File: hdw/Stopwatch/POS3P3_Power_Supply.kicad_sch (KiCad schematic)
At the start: 13 parts, among them U301 TPS62130

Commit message: started sch work
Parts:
- removed C304, C305: 22uF, Capacitors_SMD:C_1206, symbol Custom_Library:C_Custom
- added C? (x2): 10uF, Capacitors_SMD:C_1206, symbol Custom_Library:C_Custom
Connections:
- net +3V3: now also C?.1, C?.1
- net GND: now also C?.2, C?.2
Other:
- moved on the sheet: C301, C302, C303, R302, R305, TP301, U301

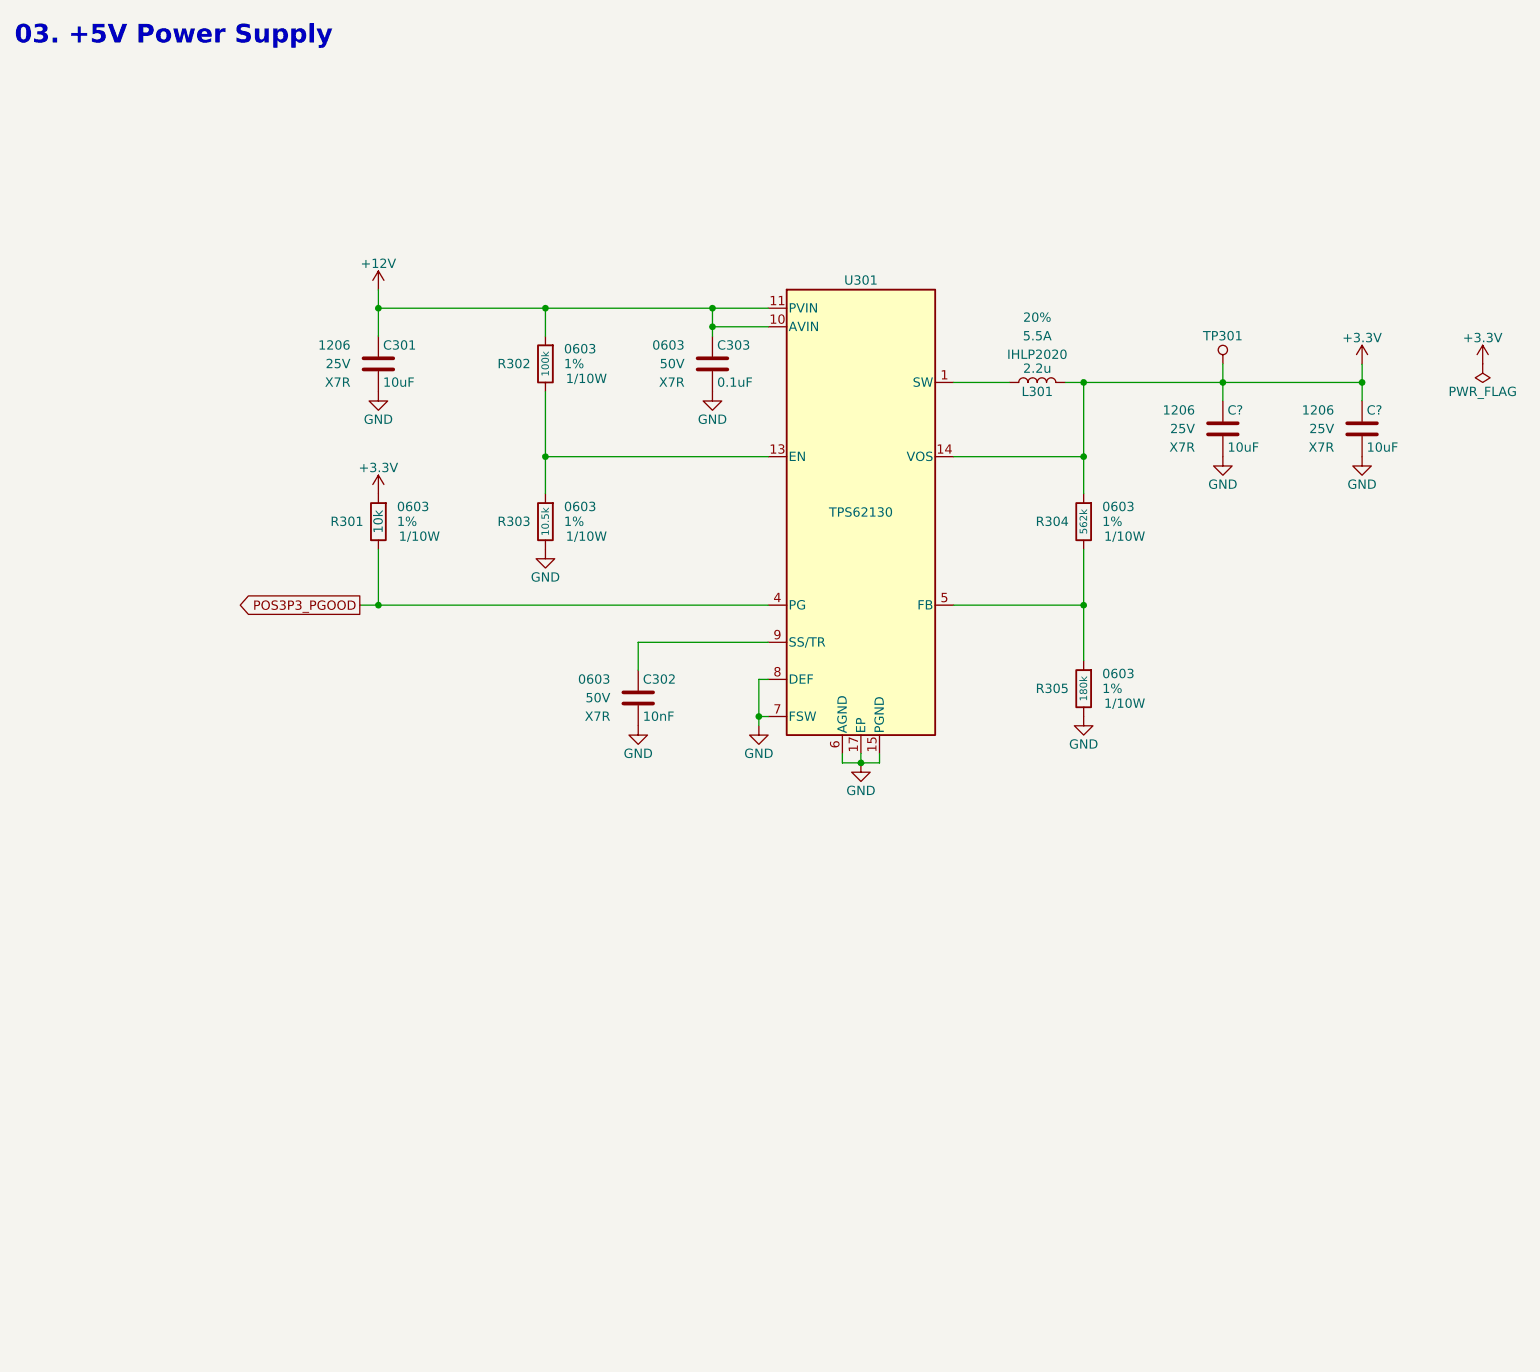
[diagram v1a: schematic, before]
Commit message: adjusted stage sheet
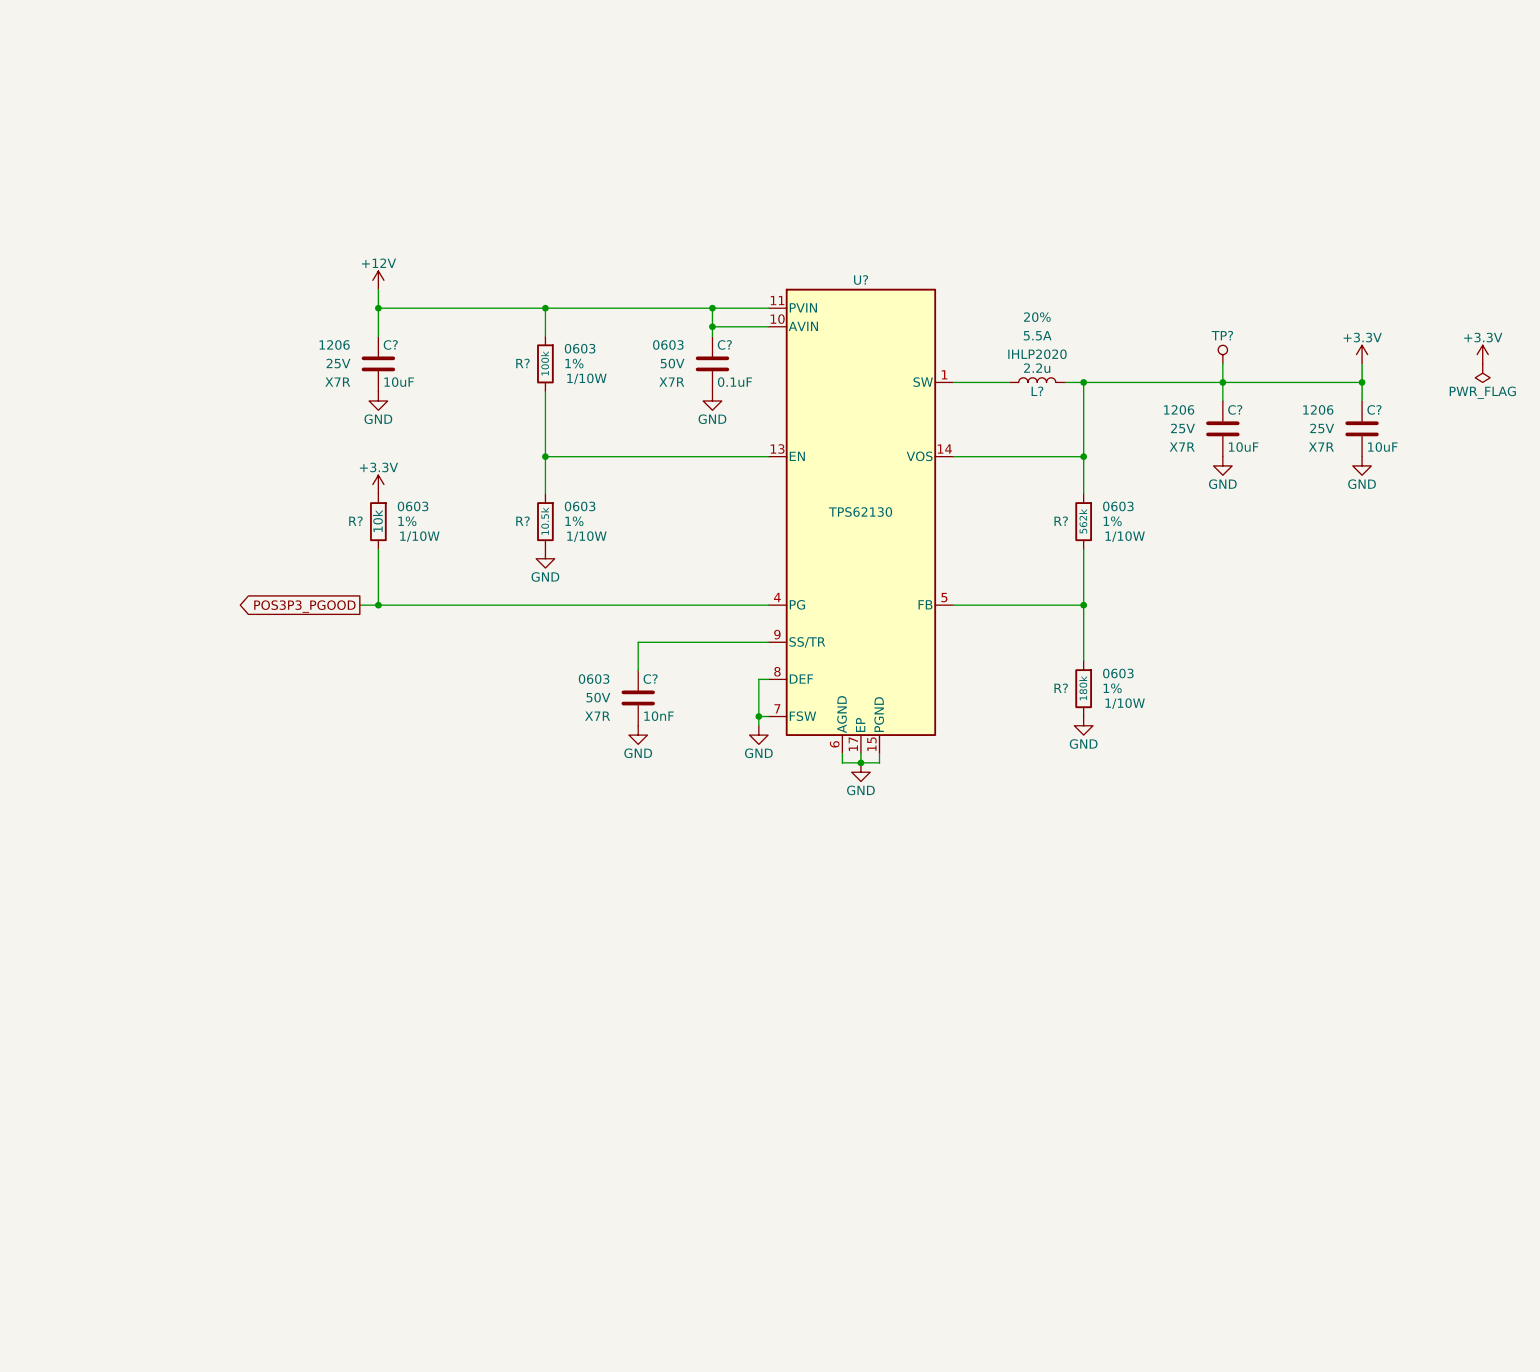
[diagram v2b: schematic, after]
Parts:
- renumbered C303 to C?, C301 to C?, C302 to C?, L301 to L?, R302 to R?, R301 to R?, R304 to R?, R305 to R?, R303 to R?, TP301 to TP?, U301 to U?
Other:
- note removed: "03. +5V Power Supply"

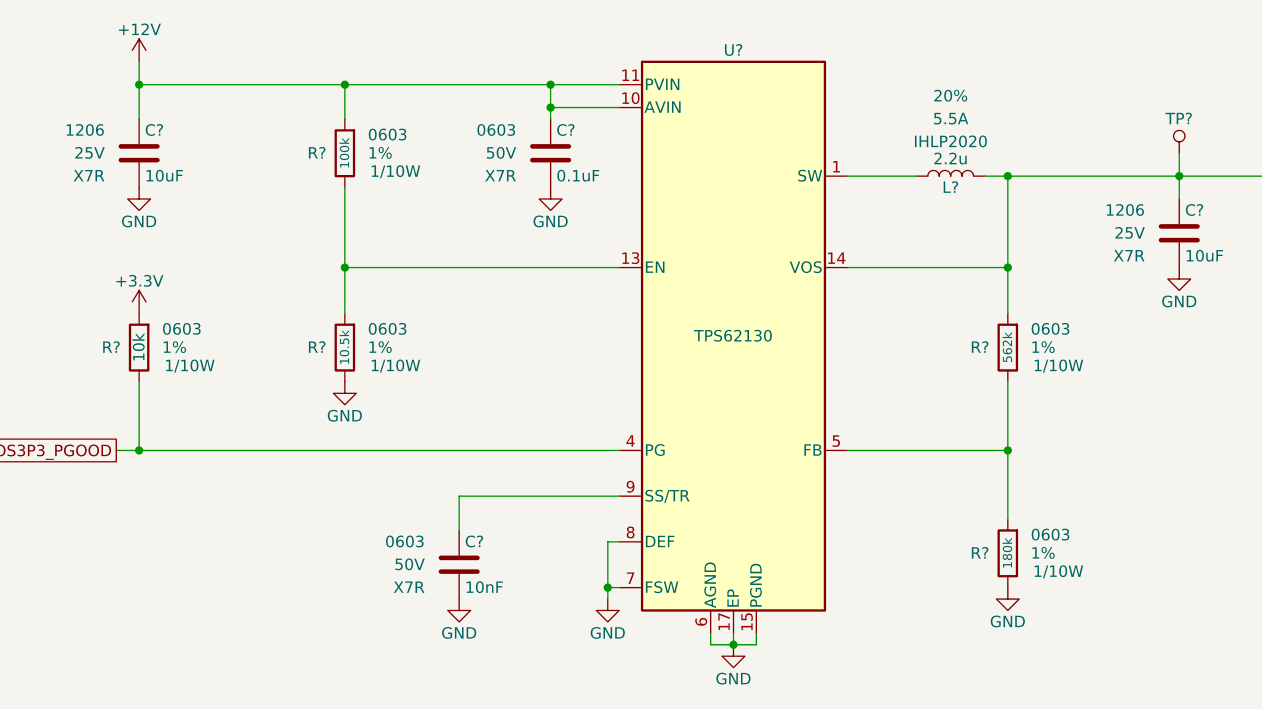
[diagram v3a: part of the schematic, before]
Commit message: Assigned some digikey pns
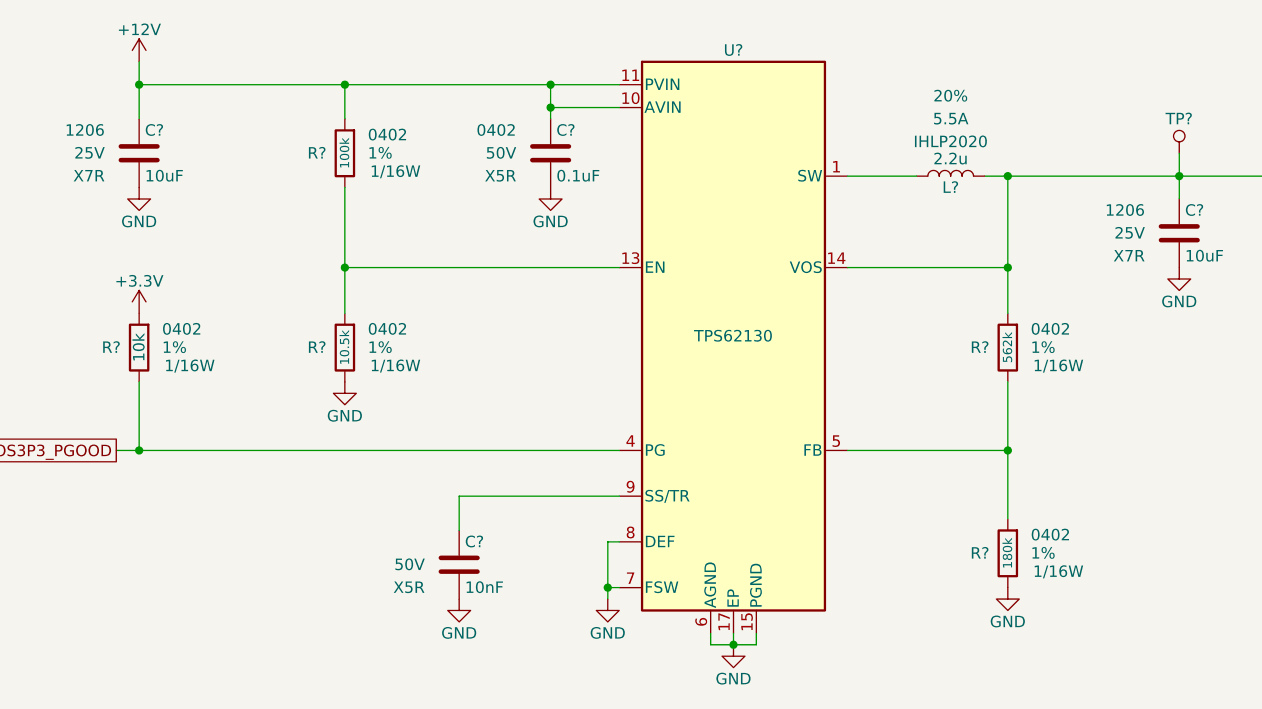
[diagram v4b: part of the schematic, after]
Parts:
- C?: footprint Capacitors_SMD:C_0603 -> Capacitors_SMD:C_0402; Dielectric X7R -> X5R; Digi-Key PN 490-8020-1-ND -> 490-10697-1-ND; display_footprint 0603 -> 0402
- C?: footprint Capacitors_SMD:C_0603 -> Capacitors_SMD:C_0402; Dielectric X7R -> X5R; Digi-Key PN 1276-1921-1-ND -> 445-12201-1-ND; display_footprint 0603 -> (none)
- R?: footprint Resistors_SMD:R_0603 -> Resistors_SMD:R_0402; Digi-Key PN A106046CT-ND -> RMCF0402FT100KCT-ND; Wattage 1/10W -> 1/16W; display_footprint 0603 -> 0402
- R?: footprint Resistors_SMD:R_0603 -> Resistors_SMD:R_0402; Digi-Key PN RHM10KADCT-ND -> RMCF0402FT10K0CT-ND; Wattage 1/10W -> 1/16W; display_footprint 0603 -> 0402
- R?: footprint Resistors_SMD:R_0603 -> Resistors_SMD:R_0402; Digi-Key PN 311-562KHRCT-ND -> RMCF0402FT562KCT-ND; Wattage 1/10W -> 1/16W; display_footprint 0603 -> 0402
- R?: footprint Resistors_SMD:R_0603 -> Resistors_SMD:R_0402; Digi-Key PN 749-1763-1-ND -> RMCF0402FT180KCT-ND; Wattage 1/10W -> 1/16W; display_footprint 0603 -> 0402
- R?: footprint Resistors_SMD:R_0603 -> Resistors_SMD:R_0402; Digi-Key PN 311-10.5KHRCT-ND -> RMCF0402FT10K5CT-ND; Wattage 1/10W -> 1/16W; display_footprint 0603 -> 0402
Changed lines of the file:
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@@
       (effects (font (size 1.27 1.27)) (justify left))
     )
-    (property "Footprint" "Capacitors_SMD:C_0603" (at 110.1852 64.77 0)
+    (property "Footprint" "Capacitors_SMD:C_0402" (at 110.1852 64.77 0)
       (effects (font (size 1.27 1.27)) hide)
     )
@@
       (effects (font (size 1.27 1.27)) hide)
     )
-    (property "display_footprint" "0603" (at 105.41 58.42 0)
+    (property "display_footprint" "0402" (at 105.41 58.42 0)
       (effects (font (size 1.27 1.27)) (justify right))
     )
@@
       (effects (font (size 1.27 1.27)) (justify right))
     )
-    (property "Dielectric" "X7R" (at 105.41 63.5 0)
-      (effects (font (size 1.27 1.27)) (justify right))
-    )
-    (property "Digi-Key PN" "490-8020-1-ND" (at 120.015 48.26 0)
+    (property "Dielectric" "X5R" (at 105.41 63.5 0)
+      (effects (font (size 1.27 1.27)) (justify right))
+    )
+    (property "Digi-Key PN" "490-10697-1-ND" (at 120.015 48.26 0)
       (effects (font (size 1.524 1.524)) hide)
     )
@@
       (effects (font (size 1.016 1.016)))
     )
-    (property "Footprint" "Resistors_SMD:R_0603" (at 86.36 60.96 0)
+    (property "Footprint" "Resistors_SMD:R_0402" (at 86.36 60.96 0)
       (effects (font (size 1.27 1.27)) hide)
     )
@@
       (effects (font (size 1.27 1.27)) hide)
     )
-    (property "display_footprint" "0603" (at 88.9 58.928 0)
+    (property "display_footprint" "0402" (at 88.9 58.928 0)
       (effects (font (size 1.27 1.27)) (justify left))
     )
@@
       (effects (font (size 1.27 1.27)) (justify left))
     )
-    (property "Wattage" "1/10W" (at 89.154 62.992 0)
-      (effects (font (size 1.27 1.27)) (justify left))
-    )
-    (property "Digi-Key PN" "A106046CT-ND" (at 0 122.428 0)
+    (property "Wattage" "1/16W" (at 89.154 62.992 0)
+      (effects (font (size 1.27 1.27)) (justify left))
+    )
+    (property "Digi-Key PN" "RMCF0402FT100KCT-ND" (at 0 122.428 0)
       (effects (font (size 1.27 1.27)) hide)
     )
@@
       (effects (font (size 1.27 1.27)))
     )
-    (property "Footprint" "Resistors_SMD:R_0603" (at 63.5 82.55 0)
+    (property "Footprint" "Resistors_SMD:R_0402" (at 63.5 82.55 0)
       (effects (font (size 1.27 1.27)) hide)
     )
@@
       (effects (font (size 1.27 1.27)) hide)
     )
-    (property "display_footprint" "0603" (at 66.04 80.518 0)
+    (property "display_footprint" "0402" (at 66.04 80.518 0)
       (effects (font (size 1.27 1.27)) (justify left))
     )
@@
       (effects (font (size 1.27 1.27)) (justify left))
     )
-    (property "Wattage" "1/10W" (at 66.294 84.582 0)
-      (effects (font (size 1.27 1.27)) (justify left))
-    )
-    (property "Digi-Key PN" "RHM10KADCT-ND" (at 71.12 72.39 0)
+    (property "Wattage" "1/16W" (at 66.294 84.582 0)
+      (effects (font (size 1.27 1.27)) (justify left))
+    )
+    (property "Digi-Key PN" "RMCF0402FT10K0CT-ND" (at 71.12 72.39 0)
       (effects (font (size 1.524 1.524)) hide)
     )
@@
       (effects (font (size 1.27 1.27)) (justify left))
     )
-    (property "Footprint" "Capacitors_SMD:C_0603" (at 100.0252 110.49 0)
+    (property "Footprint" "Capacitors_SMD:C_0402" (at 100.0252 110.49 0)
       (effects (font (size 1.27 1.27)) hide)
     )
@@
       (effects (font (size 1.27 1.27)) hide)
     )
-    (property "display_footprint" "0603" (at 95.25 104.14 0)
+    (property "display_footprint" "" (at 95.25 104.14 0)
       (effects (font (size 1.27 1.27)) (justify right))
     )
@@
       (effects (font (size 1.27 1.27)) (justify right))
     )
-    (property "Dielectric" "X7R" (at 95.25 109.22 0)
-      (effects (font (size 1.27 1.27)) (justify right))
-    )
-    (property "Digi-Key PN" "1276-1921-1-ND" (at -0.508 213.868 0)
+    (property "Dielectric" "X5R" (at 95.25 109.22 0)
+      (effects (font (size 1.27 1.27)) (justify right))
+    )
+    (property "Digi-Key PN" "445-12201-1-ND" (at -0.508 213.868 0)
       (effects (font (size 1.27 1.27)) hide)
     )
@@
       (effects (font (size 1.016 1.016)))
     )
-    (property "Footprint" "Resistors_SMD:R_0603" (at 160.02 82.55 0)
+    (property "Footprint" "Resistors_SMD:R_0402" (at 160.02 82.55 0)
       (effects (font (size 1.27 1.27)) hide)
     )
@@
       (effects (font (size 1.27 1.27)) hide)
     )
-    (property "display_footprint" "0603" (at 162.56 80.518 0)
+    (property "display_footprint" "0402" (at 162.56 80.518 0)
       (effects (font (size 1.27 1.27)) (justify left))
     )
@@
       (effects (font (size 1.27 1.27)) (justify left))
     )
-    (property "Wattage" "1/10W" (at 162.814 84.582 0)
-      (effects (font (size 1.27 1.27)) (justify left))
-    )
-    (property "Digi-Key PN" "311-562KHRCT-ND" (at 160.02 82.55 0)
+    (property "Wattage" "1/16W" (at 162.814 84.582 0)
+      (effects (font (size 1.27 1.27)) (justify left))
+    )
+    (property "Digi-Key PN" "RMCF0402FT562KCT-ND" (at 160.02 82.55 0)
       (effects (font (size 1.27 1.27)) hide)
     )
@@
       (effects (font (size 1.016 1.016)))
     )
-    (property "Footprint" "Resistors_SMD:R_0603" (at 160.02 105.41 0)
+    (property "Footprint" "Resistors_SMD:R_0402" (at 160.02 105.41 0)
       (effects (font (size 1.27 1.27)) hide)
     )
@@
       (effects (font (size 1.27 1.27)) hide)
     )
-    (property "display_footprint" "0603" (at 162.56 103.378 0)
+    (property "display_footprint" "0402" (at 162.56 103.378 0)
       (effects (font (size 1.27 1.27)) (justify left))
     )
@@
       (effects (font (size 1.27 1.27)) (justify left))
     )
-    (property "Wattage" "1/10W" (at 162.814 107.442 0)
-      (effects (font (size 1.27 1.27)) (justify left))
-    )
-    (property "Digi-Key PN" "749-1763-1-ND" (at 160.02 105.41 0)
+    (property "Wattage" "1/16W" (at 162.814 107.442 0)
+      (effects (font (size 1.27 1.27)) (justify left))
+    )
+    (property "Digi-Key PN" "RMCF0402FT180KCT-ND" (at 160.02 105.41 0)
       (effects (font (size 1.27 1.27)) hide)
     )
@@
       (effects (font (size 1.016 1.016)))
     )
-    (property "Footprint" "Resistors_SMD:R_0603" (at 86.36 82.55 0)
+    (property "Footprint" "Resistors_SMD:R_0402" (at 86.36 82.55 0)
       (effects (font (size 1.27 1.27)) hide)
     )
@@
       (effects (font (size 1.27 1.27)) hide)
     )
-    (property "display_footprint" "0603" (at 88.9 80.518 0)
+    (property "display_footprint" "0402" (at 88.9 80.518 0)
       (effects (font (size 1.27 1.27)) (justify left))
     )
@@
       (effects (font (size 1.27 1.27)) (justify left))
     )
-    (property "Wattage" "1/10W" (at 89.154 84.582 0)
-      (effects (font (size 1.27 1.27)) (justify left))
-    )
-    (property "Digi-Key PN" "311-10.5KHRCT-ND" (at 0 165.354 0)
-      (effects (font (size 1.27 1.27)) hide)
-    )
+    (property "Wattage" "1/16W" (at 89.154 84.582 0)
+      (effects (font (size 1.27 1.27)) (justify left))
+    )
+    (property "Digi-Key PN" "RMCF0402FT10K5CT-ND" (at 0 165.354 0)
+      (effects (font (size 1.27 1.27)) hide)
+    )
